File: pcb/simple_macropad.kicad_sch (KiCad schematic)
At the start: 20 parts, among them J3 OLED_128x32, SW1 RotaryEncoder_Switch, SW2 RotaryEncoder_Switch, U1 Seeed Studio XIAO SAMD21

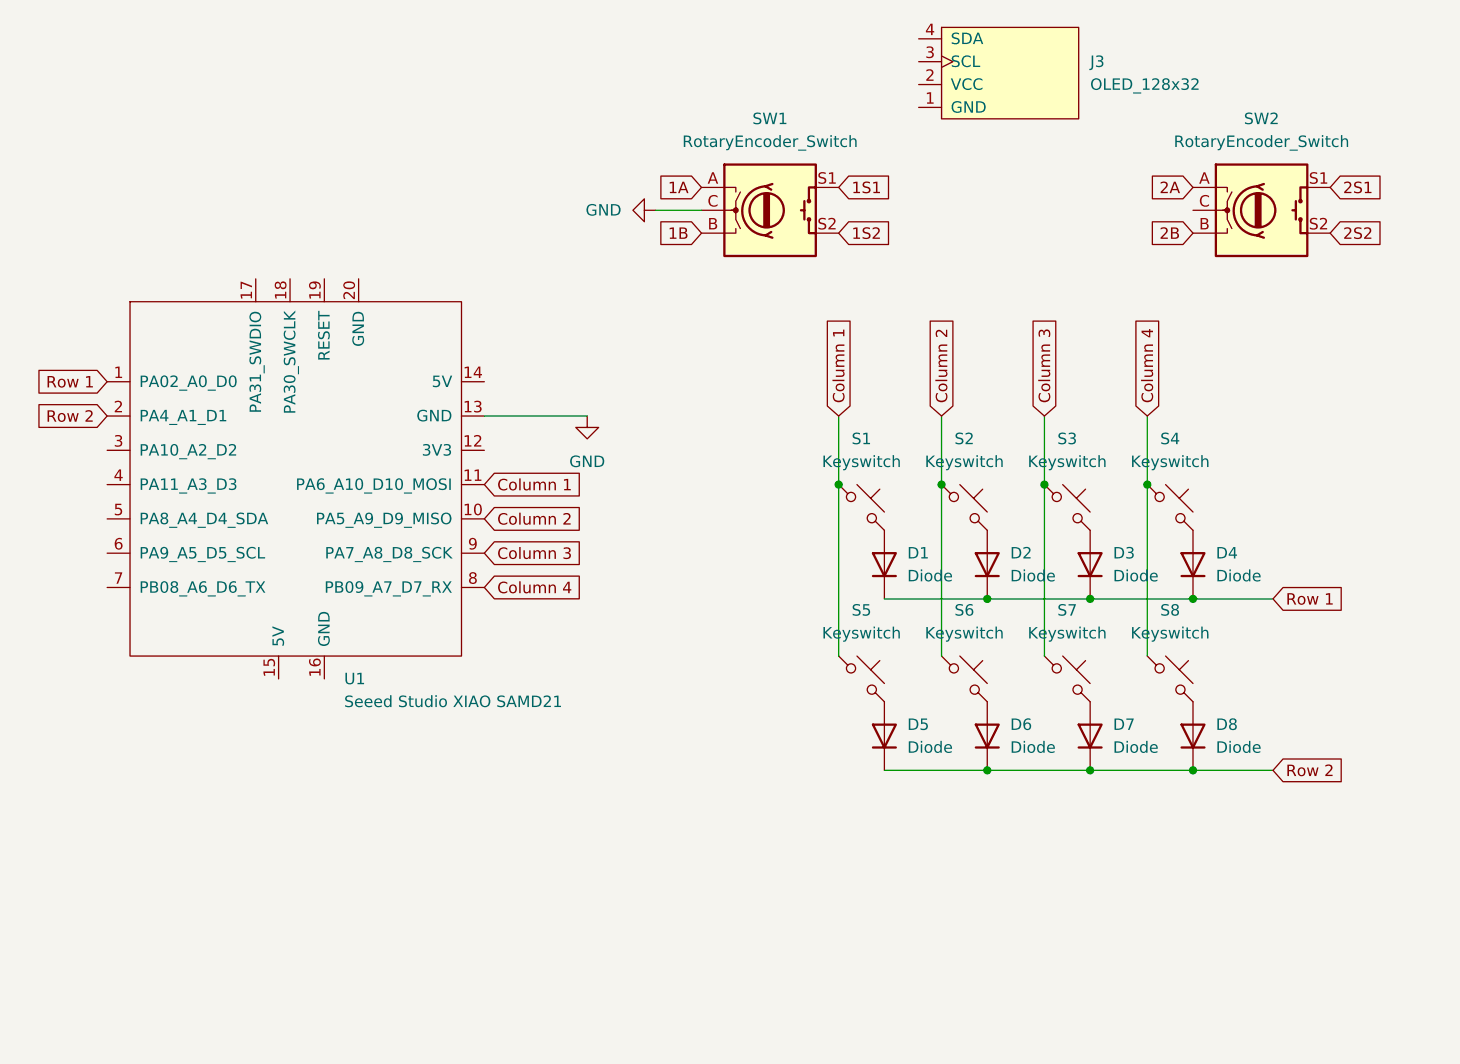
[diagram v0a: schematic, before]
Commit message: added footprints
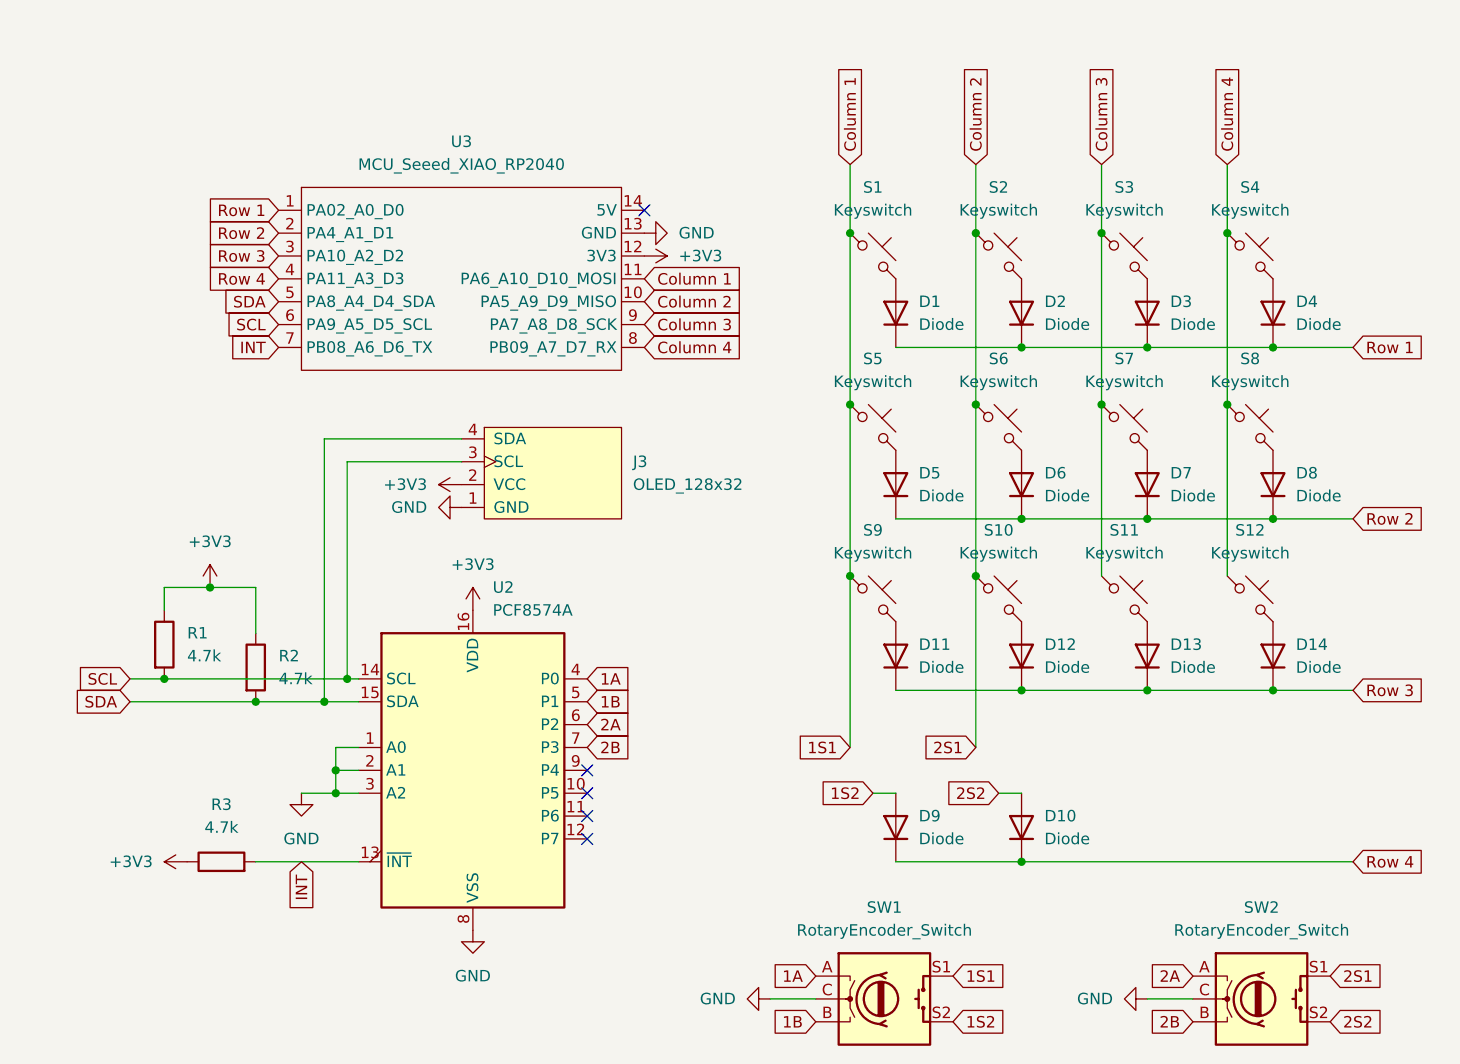
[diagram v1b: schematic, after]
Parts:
- removed U1: Seeed Studio XIAO SAMD21, symbol Seeed_Studio_XIAO_Series:Seeed Studio XIAO SAMD21
- added D10, D11, D12, D13, D14, D9: Diode, ScottoKeebs_Components:Diode_DO-35, symbol ScottoKeebs:Placeholder_Diode
- added R1, R2, R3: 4.7k, Resistor_THT:R_Axial_DIN0207_L6.3mm_D2.5mm_P10.16mm_Horizontal, symbol Device:R
- added S10, S11, S12, S9: Keyswitch, ScottoKeebs_MX:MX_PCB_1.00u, symbol ScottoKeebs:Placeholder_Keyswitch
- added U2: PCF8574A, Package_DIP:DIP-16_W7.62mm, symbol Interface_Expansion:PCF8574A
- added U3: MCU_Seeed_XIAO_RP2040, ScottoKeebs_MCU:Seeed_XIAO_RP2040, symbol ScottoKeebs:MCU_Seeed_XIAO_RP2040
- D1, D2, D3, D4, D5, D6, D7, D8: footprint (none) -> ScottoKeebs_Components:Diode_DO-35
- S1, S2, S3, S4, S5, S6, S7, S8: footprint (none) -> ScottoKeebs_MX:MX_PCB_1.00u
- SW1, SW2: footprint (none) -> Rotary_Encoder:RotaryEncoder_Alps_EC11E_Vertical_H20mm
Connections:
- net Column 1 is gone; now on net 1S1: S1.1, S5.1
- net Column 2 is gone; now on net 2S1: S2.1, S6.1
- net 1A: now also U2.4 (P0)
- net 1B: now also U2.5 (P1)
- net 1S1: now also S9.1, U3.11 (PA6_A10_D10_MOSI)
- net 1S2: now also D9.2 (A)
- net 2A: now also U2.6 (P2)
- net 2B: now also U2.7 (P3)
- net 2S1: now also S10.1, U3.10 (PA5_A9_D9_MISO)
- net 2S2: now also D10.2 (A)
- net Column 3: now also S11.1, U3.9 (PA7_A8_D8_SCK)
- net Column 4: now also S12.1, U3.8 (PB09_A7_D7_RX)
- net GND: now also J3.1 (GND), SW2.C, U2.1 (A0), U2.2 (A1), U2.3 (A2), U2.8 (VSS), U3.13 (GND)
- net Row 1: now also U3.1 (PA02_A0_D0)
- net Row 2: now also U3.2 (PA4_A1_D1)
- net +3V3: now reaches J3.2 (VCC)
- net +3V3: now also R1.1, R2.1, R3.1, U2.16 (VDD), U3.12 (3V3)
- net SCL: now reaches J3.3 (SCL)
- net SCL: now also R1.2, U2.14 (SCL), U3.6 (PA9_A5_D5_SCL)
- net SDA: now reaches J3.4 (SDA)
- net SDA: now also R2.2, U2.15 (SDA), U3.5 (PA8_A4_D4_SDA)
- new net: D14.2 (A), S12.2
- new net: D12.2 (A), S10.2
- new net: D11.2 (A), S9.2
- new net: D13.2 (A), S11.2
- new net INT: R3.2, U2.13 (~{INT}), U3.7 (PB08_A6_D6_TX)
- new net Row 3: D11.1 (K), D12.1 (K), D13.1 (K), D14.1 (K), U3.3 (PA10_A2_D2)
- new net Row 4: D10.1 (K), D9.1 (K), U3.4 (PA11_A3_D3)
- no-connect marks 0 -> 5
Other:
- moved on the sheet: D1, D2, D3, D4, D5, D6, D7, D8, J3, S1, S2, S3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

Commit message: wired components in pcb
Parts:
- SW1, SW2: footprint Rotary_Encoder:RotaryEncoder_Alps_EC11E_Vertical_H20mm -> Rotary_Encoder:RotaryEncoder_Alps_EC11E-Switch_Vertical_H20mm
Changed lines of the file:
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@@
 			)
 		)
-		(property "Footprint" "Rotary_Encoder:RotaryEncoder_Alps_EC11E_Vertical_H20mm"
+		(property "Footprint" "Rotary_Encoder:RotaryEncoder_Alps_EC11E-Switch_Vertical_H20mm"
 			(at 223.52 136.906 0)
 			(effects
@@
 			)
 		)
-		(property "Footprint" "Rotary_Encoder:RotaryEncoder_Alps_EC11E_Vertical_H20mm"
+		(property "Footprint" "Rotary_Encoder:RotaryEncoder_Alps_EC11E-Switch_Vertical_H20mm"
 			(at 181.61 136.906 0)
 			(effects
